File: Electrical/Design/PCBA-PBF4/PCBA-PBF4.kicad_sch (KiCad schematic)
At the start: 0 parts

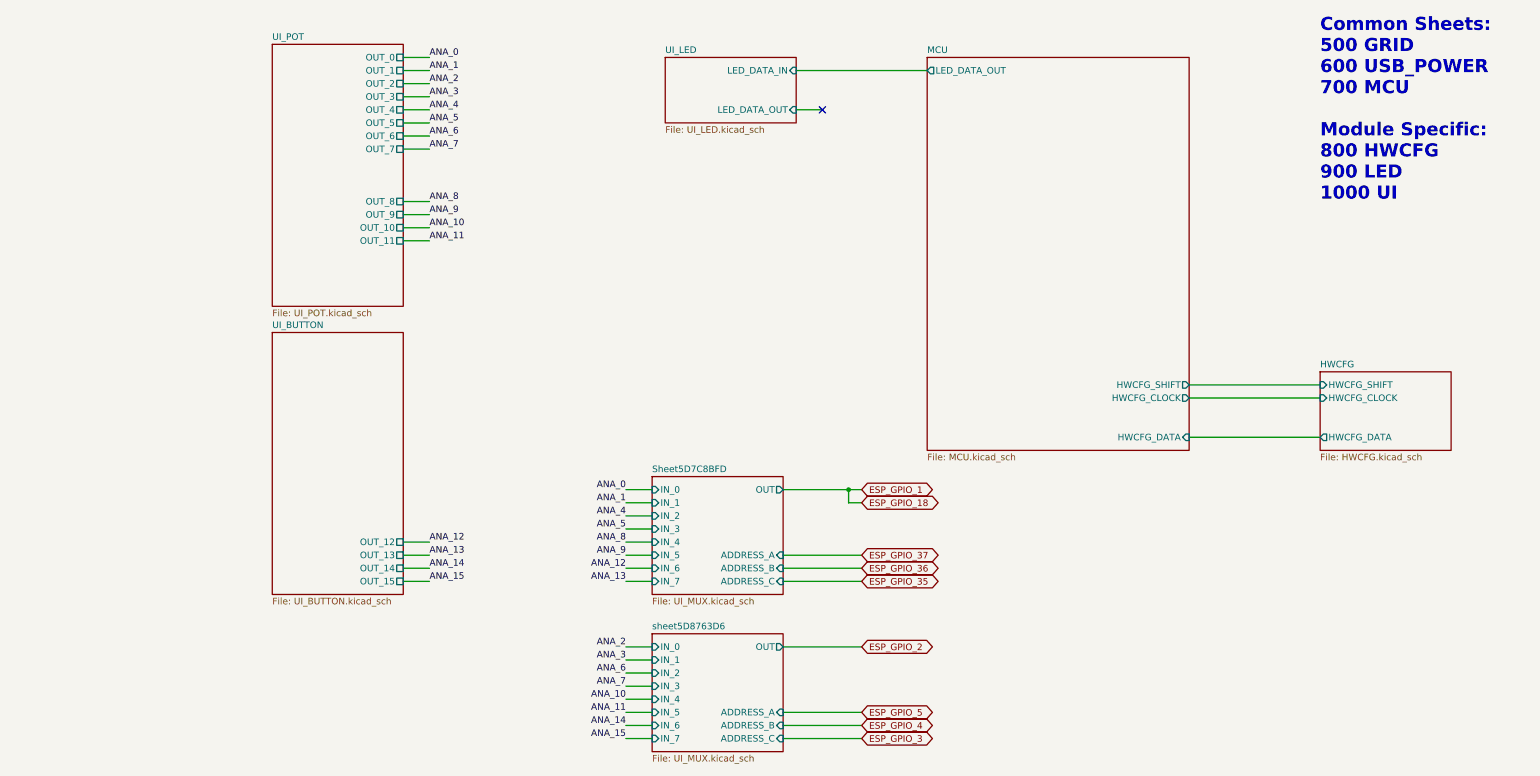
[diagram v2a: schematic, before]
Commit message: SUKU design updated to use hall based switch
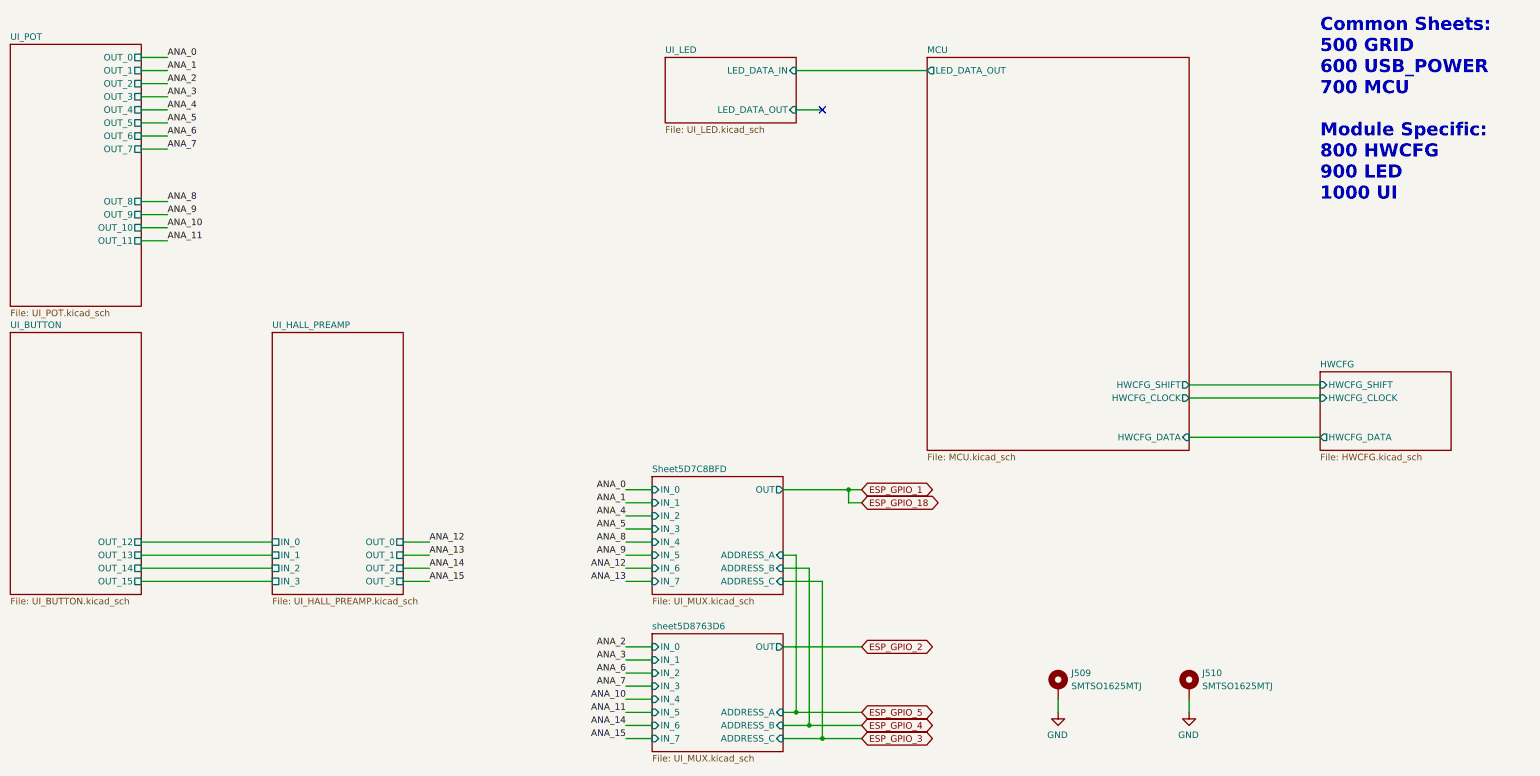
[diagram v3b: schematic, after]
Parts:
- added J509, J510: SMTSO1625MTJ, suku_basics:SMD_NUT_M1.6x2.5, symbol suku_basics:SMD_NUT
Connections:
- new net GND: J509.1, J510.1
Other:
- added sheet UI_HALL_PREAMP (UI_HALL_PREAMP.kicad_sch)
